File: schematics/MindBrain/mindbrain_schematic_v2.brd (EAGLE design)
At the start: 92.4 x 49.5 mm, 51 parts, among them CON1 POWER, IC1 TL084P, IC2 TL084P

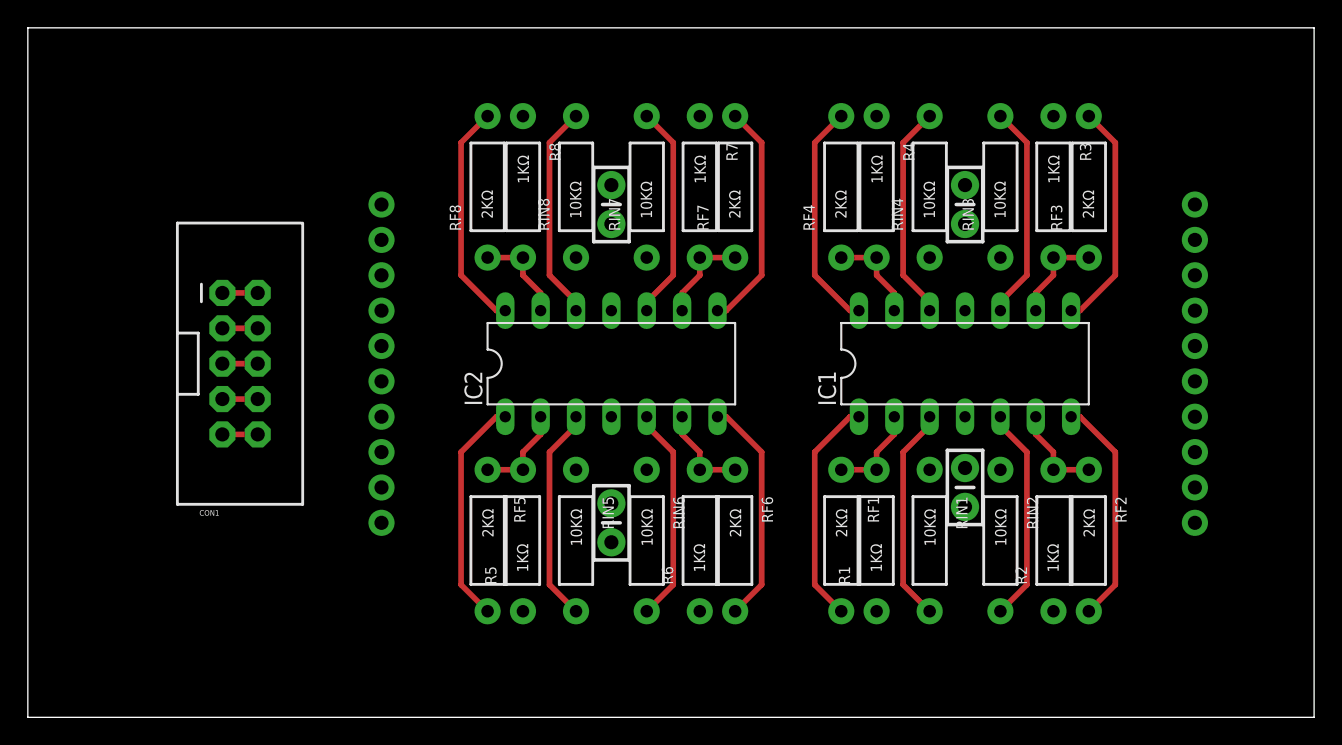
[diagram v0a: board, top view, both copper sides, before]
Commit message: trying to split traces between top and bottom layers
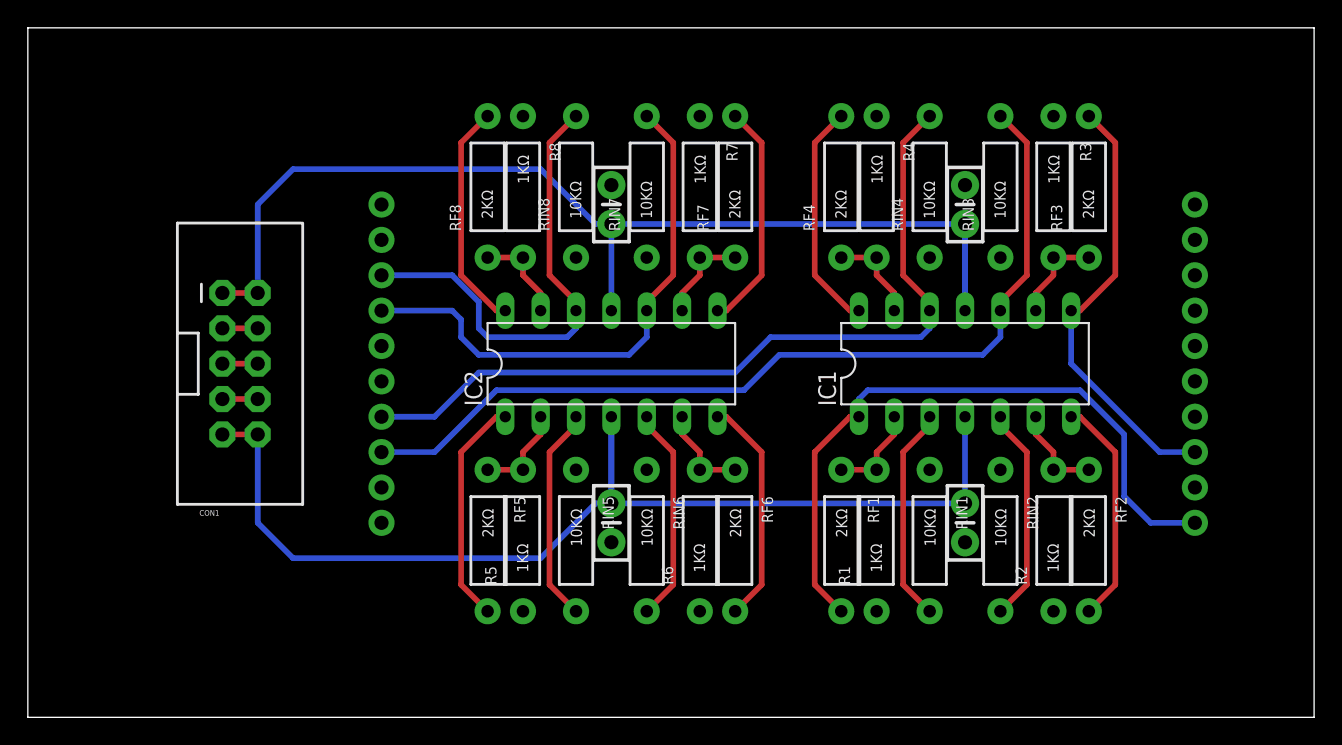
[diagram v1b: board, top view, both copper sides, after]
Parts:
- moved C3 2.54 mm to (67.3, 14.0)
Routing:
- net N$27: track 2.54 -> 81.9 mm
- net N$25: track 2.54 -> 81.2 mm
- net N$7: track 15.5 -> 65.3 mm
- net N$10: track 15.5 -> 58.8 mm
- net N$2: track 16.4 -> 48.7 mm
- net N$19: track 15.5 -> 39.1 mm
- net N$22: track 15.5 -> 34.0 mm
- net N$8: track 16.4 -> 31.8 mm

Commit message: Got all traces except gnds using vias
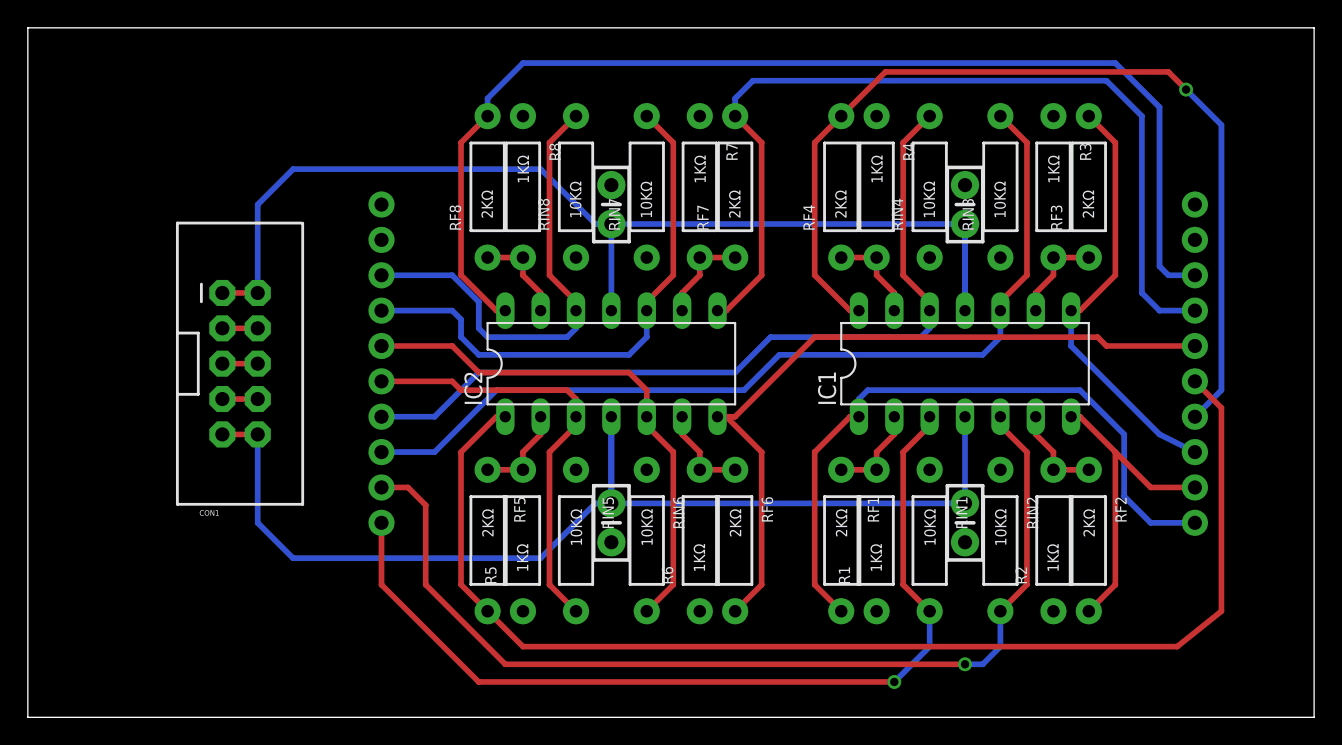
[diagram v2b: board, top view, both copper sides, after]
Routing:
- net N$14: track 16.4 -> 88.4 mm
- net N$23: track 16.4 -> 82.6 mm
- net N$4: track 15.5 -> 71.7 mm, vias 0 -> 1
- net N$11: track 16.4 -> 68.4 mm, vias 0 -> 1
- net N$1: track 15.5 -> 65.8 mm, vias 0 -> 1
- net N$20: track 16.4 -> 65.5 mm
- net N$17: track 16.4 -> 53.4 mm
- net N$16: track 15.5 -> 37.8 mm
- net N$13: track 15.5 -> 31.3 mm
- net N$5: track 16.4 -> 23.2 mm
- net N$8: track 31.8 -> 30.8 mm
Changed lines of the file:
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@@
 <wire x1="62.865" y1="19.05" x2="64.77" y2="20.955" width="0.4064" layer="1"/>
 <wire x1="64.77" y1="20.955" x2="64.77" y2="21.59" width="0.4064" layer="1"/>
-<wire x1="25.4" y1="13.97" x2="62.865" y2="9.525" width="0" layer="19" extent="1-1"/>
+<wire x1="25.4" y1="13.97" x2="25.4" y2="9.525" width="0.4064" layer="1"/>
+<wire x1="25.4" y1="9.525" x2="32.385" y2="2.54" width="0.4064" layer="1"/>
+<wire x1="32.385" y1="2.54" x2="62.23" y2="2.54" width="0.4064" layer="1"/>
+<via x="62.23" y="2.54" extent="1-16" drill="0.6" shape="square"/>
+<wire x1="62.23" y1="2.54" x2="64.77" y2="5.08" width="0.4064" layer="16"/>
+<wire x1="64.77" y1="5.08" x2="64.77" y2="7.62" width="0.4064" layer="16"/>
 </signal>
 <signal name="GND">
@@
 <wire x1="71.755" y1="19.05" x2="69.85" y2="20.955" width="0.4064" layer="1"/>
 <wire x1="69.85" y1="20.955" x2="69.85" y2="21.59" width="0.4064" layer="1"/>
-<wire x1="25.4" y1="16.51" x2="69.85" y2="20.955" width="0" layer="19" extent="1-1"/>
+<wire x1="25.4" y1="16.51" x2="27.305" y2="16.51" width="0.4064" layer="1"/>
+<wire x1="27.305" y1="16.51" x2="28.575" y2="15.24" width="0.4064" layer="1"/>
+<wire x1="28.575" y1="15.24" x2="28.575" y2="9.525" width="0.4064" layer="1"/>
+<wire x1="28.575" y1="9.525" x2="34.29" y2="3.81" width="0.4064" layer="1"/>
+<wire x1="34.29" y1="3.81" x2="67.31" y2="3.81" width="0.4064" layer="1"/>
+<via x="67.31" y="3.81" extent="1-16" drill="0.6" shape="square"/>
+<wire x1="67.31" y1="3.81" x2="68.58" y2="3.81" width="0.4064" layer="16"/>
+<wire x1="68.58" y1="3.81" x2="69.85" y2="5.08" width="0.4064" layer="16"/>
+<wire x1="69.85" y1="5.08" x2="69.85" y2="7.62" width="0.4064" layer="16"/>
 </signal>
 <signal name="N$5">
@@
 <wire x1="78.105" y1="19.05" x2="75.565" y2="21.59" width="0.4064" layer="1"/>
 <wire x1="75.565" y1="21.59" x2="74.93" y2="21.59" width="0.4064" layer="1"/>
-<wire x1="78.105" y1="19.05" x2="83.82" y2="16.51" width="0" layer="19" extent="1-1"/>
+<wire x1="83.82" y1="16.51" x2="80.645" y2="16.51" width="0.4064" layer="1"/>
+<wire x1="80.645" y1="16.51" x2="78.105" y2="19.05" width="0.4064" layer="1"/>
 </signal>
 <signal name="N$6">
@@
 <wire x1="78.105" y1="31.75" x2="75.565" y2="29.21" width="0.4064" layer="1"/>
 <wire x1="75.565" y1="29.21" x2="74.93" y2="29.21" width="0.4064" layer="1"/>
-<wire x1="83.82" y1="19.05" x2="81.28" y2="19.05" width="0.4064" layer="16"/>
-<wire x1="81.28" y1="19.05" x2="74.93" y2="25.4" width="0.4064" layer="16"/>
-<wire x1="74.93" y1="25.4" x2="74.93" y2="29.21" width="0.4064" layer="16"/>
+<wire x1="83.82" y1="19.05" x2="81.28" y2="20.32" width="0.4064" layer="16"/>
+<wire x1="81.28" y1="20.32" x2="74.93" y2="26.67" width="0.4064" layer="16"/>
+<wire x1="74.93" y1="26.67" x2="74.93" y2="29.21" width="0.4064" layer="16"/>
 </signal>
 <signal name="N$9">
@@
 <wire x1="56.515" y1="31.75" x2="59.055" y2="29.21" width="0.4064" layer="1"/>
 <wire x1="59.055" y1="29.21" x2="59.69" y2="29.21" width="0.4064" layer="1"/>
-<wire x1="59.69" y1="29.21" x2="83.82" y2="21.59" width="0" layer="19" extent="1-1"/>
+<wire x1="83.82" y1="21.59" x2="85.725" y2="23.495" width="0.4064" layer="16"/>
+<wire x1="85.725" y1="23.495" x2="85.725" y2="42.545" width="0.4064" layer="16"/>
+<wire x1="85.725" y1="42.545" x2="83.185" y2="45.085" width="0.4064" layer="16"/>
+<via x="83.185" y="45.085" extent="1-16" drill="0.6" shape="square"/>
+<wire x1="83.185" y1="45.085" x2="81.915" y2="46.355" width="0.4064" layer="1"/>
+<wire x1="81.915" y1="46.355" x2="61.595" y2="46.355" width="0.4064" layer="1"/>
+<wire x1="61.595" y1="46.355" x2="58.42" y2="43.18" width="0.4064" layer="1"/>
 </signal>
 <signal name="N$12">
@@
 <wire x1="37.465" y1="19.05" x2="39.37" y2="20.955" width="0.4064" layer="1"/>
 <wire x1="39.37" y1="20.955" x2="39.37" y2="21.59" width="0.4064" layer="1"/>
-<wire x1="37.465" y1="19.05" x2="25.4" y2="24.13" width="0" layer="19" extent="1-1"/>
+<wire x1="25.4" y1="24.13" x2="30.48" y2="24.13" width="0.4064" layer="1"/>
+<wire x1="30.48" y1="24.13" x2="31.115" y2="23.495" width="0.4064" layer="1"/>
+<wire x1="31.115" y1="23.495" x2="38.735" y2="23.495" width="0.4064" layer="1"/>
+<wire x1="38.735" y1="23.495" x2="39.37" y2="22.86" width="0.4064" layer="1"/>
+<wire x1="39.37" y1="22.86" x2="39.37" y2="21.59" width="0.4064" layer="1"/>
 </signal>
 <signal name="N$14">
@@
 <wire x1="31.115" y1="19.05" x2="33.655" y2="21.59" width="0.4064" layer="1"/>
 <wire x1="33.655" y1="21.59" x2="34.29" y2="21.59" width="0.4064" layer="1"/>
-<wire x1="34.29" y1="21.59" x2="83.82" y2="24.13" width="0" layer="19" extent="1-1"/>
+<wire x1="83.82" y1="24.13" x2="85.725" y2="22.225" width="0.4064" layer="1"/>
+<wire x1="85.725" y1="22.225" x2="85.725" y2="7.62" width="0.4064" layer="1"/>
+<wire x1="85.725" y1="7.62" x2="82.55" y2="5.08" width="0.4064" layer="1"/>
+<wire x1="82.55" y1="5.08" x2="35.56" y2="5.08" width="0.4064" layer="1"/>
+<wire x1="35.56" y1="5.08" x2="33.02" y2="7.62" width="0.4064" layer="1"/>
 </signal>
 <signal name="N$15">
@@
 <wire x1="46.355" y1="19.05" x2="44.45" y2="20.955" width="0.4064" layer="1"/>
 <wire x1="44.45" y1="20.955" x2="44.45" y2="21.59" width="0.4064" layer="1"/>
-<wire x1="44.45" y1="21.59" x2="25.4" y2="26.67" width="0" layer="19" extent="1-1"/>
+<wire x1="25.4" y1="26.67" x2="30.48" y2="26.67" width="0.4064" layer="1"/>
+<wire x1="30.48" y1="26.67" x2="32.385" y2="24.765" width="0.4064" layer="1"/>
+<wire x1="32.385" y1="24.765" x2="43.18" y2="24.765" width="0.4064" layer="1"/>
+<wire x1="43.18" y1="24.765" x2="44.45" y2="23.495" width="0.4064" layer="1"/>
+<wire x1="44.45" y1="23.495" x2="44.45" y2="21.59" width="0.4064" layer="1"/>
 </signal>
 <signal name="N$17">
@@
 <wire x1="52.705" y1="19.05" x2="50.165" y2="21.59" width="0.4064" layer="1"/>
 <wire x1="50.165" y1="21.59" x2="49.53" y2="21.59" width="0.4064" layer="1"/>
-<wire x1="52.705" y1="19.05" x2="83.82" y2="26.67" width="0" layer="19" extent="1-1"/>
+<wire x1="83.82" y1="26.67" x2="77.47" y2="26.67" width="0.4064" layer="1"/>
+<wire x1="77.47" y1="26.67" x2="76.835" y2="27.305" width="0.4064" layer="1"/>
+<wire x1="76.835" y1="27.305" x2="56.515" y2="27.305" width="0.4064" layer="1"/>
+<wire x1="56.515" y1="27.305" x2="50.8" y2="21.59" width="0.4064" layer="1"/>
+<wire x1="50.8" y1="21.59" x2="49.53" y2="21.59" width="0.4064" layer="1"/>
 </signal>
 <signal name="N$18">
@@
 <wire x1="52.705" y1="31.75" x2="50.165" y2="29.21" width="0.4064" layer="1"/>
 <wire x1="50.165" y1="29.21" x2="49.53" y2="29.21" width="0.4064" layer="1"/>
-<wire x1="52.705" y1="31.75" x2="83.82" y2="29.21" width="0" layer="19" extent="1-1"/>
+<wire x1="83.82" y1="29.21" x2="81.28" y2="29.21" width="0.4064" layer="16"/>
+<wire x1="81.28" y1="29.21" x2="80.01" y2="30.48" width="0.4064" layer="16"/>
+<wire x1="80.01" y1="30.48" x2="80.01" y2="43.18" width="0.4064" layer="16"/>
+<wire x1="80.01" y1="43.18" x2="77.47" y2="45.72" width="0.4064" layer="16"/>
+<wire x1="77.47" y1="45.72" x2="52.07" y2="45.72" width="0.4064" layer="16"/>
+<wire x1="52.07" y1="45.72" x2="50.8" y2="44.45" width="0.4064" layer="16"/>
+<wire x1="50.8" y1="44.45" x2="50.8" y2="43.18" width="0.4064" layer="16"/>
 </signal>
 <signal name="N$21">
@@
 <wire x1="31.115" y1="31.75" x2="33.655" y2="29.21" width="0.4064" layer="1"/>
 <wire x1="33.655" y1="29.21" x2="34.29" y2="29.21" width="0.4064" layer="1"/>
-<wire x1="34.29" y1="29.21" x2="83.82" y2="31.75" width="0" layer="19" extent="1-1"/>
+<wire x1="83.82" y1="31.75" x2="81.915" y2="31.75" width="0.4064" layer="16"/>
+<wire x1="81.915" y1="31.75" x2="81.28" y2="32.385" width="0.4064" layer="16"/>
+<wire x1="81.28" y1="32.385" x2="81.28" y2="43.815" width="0.4064" layer="16"/>
+<wire x1="81.28" y1="43.815" x2="78.105" y2="46.99" width="0.4064" layer="16"/>
+<wire x1="78.105" y1="46.99" x2="35.56" y2="46.99" width="0.4064" layer="16"/>
+<wire x1="35.56" y1="46.99" x2="33.02" y2="44.45" width="0.4064" layer="16"/>
+<wire x1="33.02" y1="44.45" x2="33.02" y2="43.18" width="0.4064" layer="16"/>
 </signal>
 <signal name="N$24">

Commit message: trying to fix merge conflicts
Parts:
- moved RF5 8.89 mm to (24.1, 12.7)
- moved RF8 8.89 mm to (24.1, 38.1)
- moved C2 8.89 mm to (58.4, 36.8)
- moved C3 8.89 mm to (58.4, 14.0)
- moved CON1 8.89 mm to (6.35, 25.4)
- moved IC1 8.89 mm to (58.4, 25.4)
- moved R1 8.89 mm to (52.1, 12.7)
- moved R2 8.89 mm to (64.8, 12.7)
- moved R3 8.89 mm to (64.8, 38.1)
- moved R4 8.89 mm to (52.1, 38.1)
- moved R5 8.89 mm to (26.7, 12.7)
- moved R6 8.89 mm to (39.4, 12.7)
- moved R7 8.89 mm to (39.4, 38.1)
- moved R8 8.89 mm to (26.7, 38.1)
- moved RF1 8.89 mm to (49.5, 12.7)
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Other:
- board size 92.4 x 49.5 mm -> 81 x 49.5 mm
